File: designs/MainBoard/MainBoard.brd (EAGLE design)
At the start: 86 x 37 mm, 6 parts

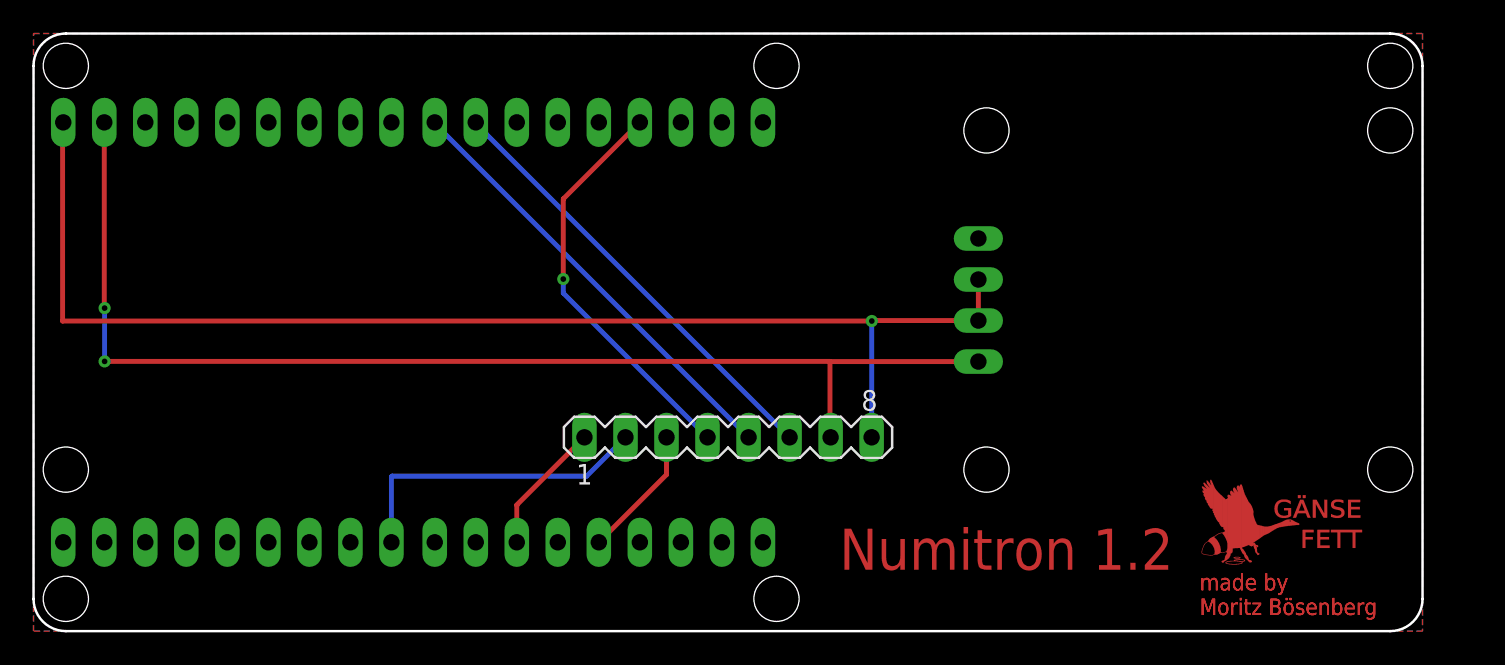
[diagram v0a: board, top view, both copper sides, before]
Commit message: added correct measurements
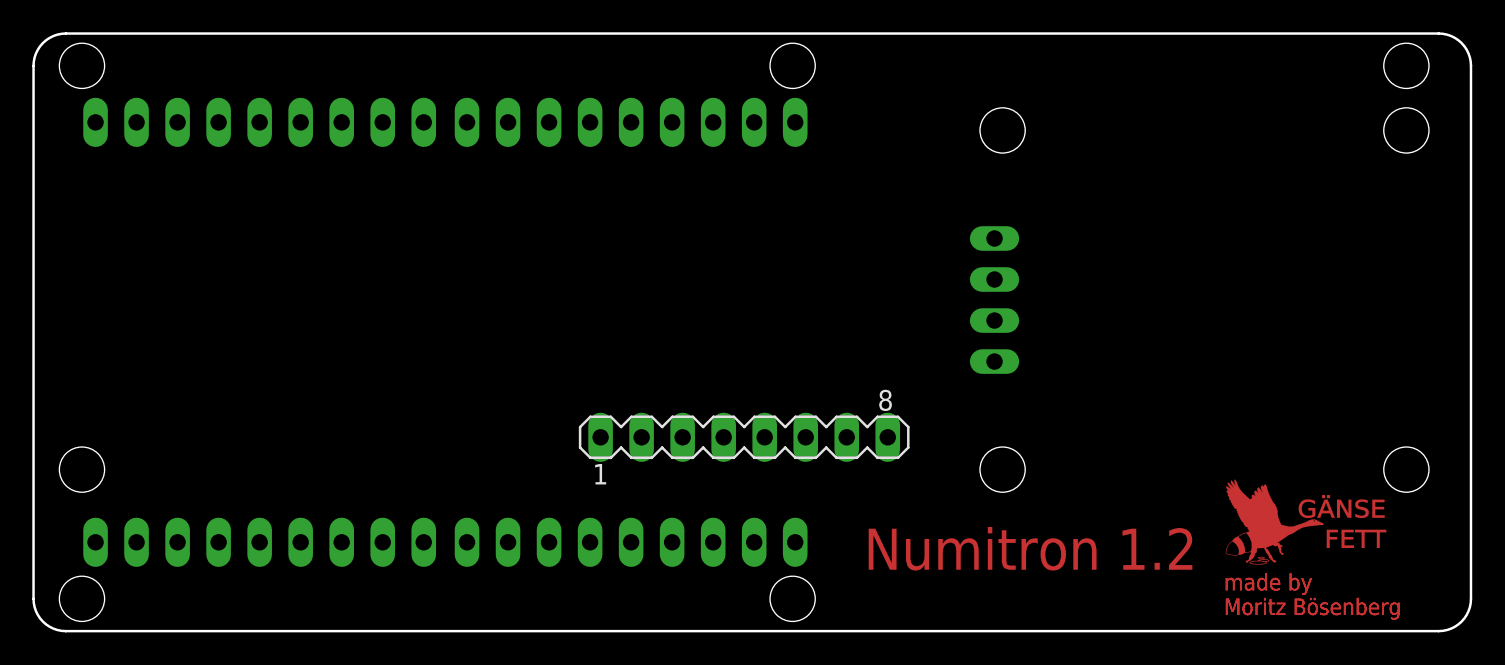
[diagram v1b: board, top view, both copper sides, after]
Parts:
- moved SV2 2.00 mm to (37.0, 5.50)
- moved SV3 2.00 mm to (14.0, 5.50)
- moved SV5 2.00 mm to (14.0, 31.5)
- moved SV6 2.00 mm to (37.0, 31.5)
- moved JP1 1.00 mm to (59.5, 20.5)
- moved SV1 1.00 mm to (44.0, 12.0)
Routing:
- net GND: track 78.8 -> 0.00 mm, vias 1 -> 0
- net 3.3V: track 73.6 -> 0.00 mm, vias 2 -> 0
- net IO26: track 27.5 -> 0.00 mm
- net IO25: track 27.5 -> 0.00 mm
- net GPIO13: track 25.2 -> 0.00 mm, vias 1 -> 0
- net IO5: track 19.6 -> 0.00 mm
- net IO4: track 8.24 -> 0.00 mm
- net IO2: track 8.24 -> 0.00 mm
- removed copper zone on layer 1, net GND
- removed copper zone on layer 16, net GND
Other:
- board size 86 x 37 mm -> 89 x 37 mm

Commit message: finished mainboard
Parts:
- removed SV1: (no value), con-lstb:MA08-1
- added J1, J2, J3, J4, J5, J6, J7, J8: S2B-PH-SM4, CommonParts:JST_S2B-PH-SM4-TB(LF)(SN)
- added R1, R2, R3, R4: (no value), CommonParts:R1206
- added SV4: (no value), CommonParts:MA08-1
- moved JP1 1.00 mm to (58.5, 20.5)
- moved SV2 1.00 mm to (36.0, 5.50)
- moved SV3 1.00 mm to (13.0, 5.50)
- moved SV5 1.00 mm to (13.0, 31.5)
- moved SV6 1.00 mm to (36.0, 31.5)
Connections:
- net 3.3V: now also J2.1, J4.1, J6.1, J8.1, R1.1, R2.1, R3.1, R4.1, SV4.7; no longer SV1.7
- net GND: now also J1.2, J2.2, J3.2, J4.2, J5.2, J6.2, J7.2, J8.2, SV4.8; no longer SV1.8
- net GPIO13: now also SV4.4; no longer SV1.4
- net IO15: now also J1.1, R1.2
- net IO2: now also SV4.3; no longer SV1.3
- net IO22: now also J7.1, R4.2
- net IO25: now also SV4.5; no longer SV1.5
- net IO26: now also SV4.6; no longer SV1.6
- net IO4: now also SV4.1; no longer SV1.1
- net IO5: now also SV4.2; no longer SV1.2
- net RXD0: now also J3.1, R2.2
- net TXD0: now also J5.1, R3.2
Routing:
- net GND: track 0.00 -> 173.4 mm, vias 0 -> 3
- net 3.3V: track 0.00 -> 119.9 mm, vias 0 -> 3
- net TXD0: track 0.00 -> 100.5 mm, vias 0 -> 4
- net IO22: track 0.00 -> 89.8 mm
- net RXD0: track 0.00 -> 87.3 mm, vias 0 -> 3
- net IO15: track 0.00 -> 52.1 mm, vias 0 -> 1
- net GPIO13: track 0.00 -> 49.7 mm, vias 0 -> 1
- net IO25: track 0.00 -> 35.6 mm, vias 0 -> 1
- net IO26: track 0.00 -> 34.7 mm, vias 0 -> 1
- net IO4: track 0.00 -> 18.6 mm
- net IO5: track 0.00 -> 17.9 mm
- net IO2: track 0.00 -> 8.36 mm
- added copper zone on layer 1, net GND
- added copper zone on layer 16, net GND
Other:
- board size 89 x 37 mm -> 86 x 37 mm
- board text added: "3.3V"
- board text added: "CLK"
- board text added: "CMD"
- board text added: "GND"
- board text added: "GPIO12"
- board text added: "GPIO13"
- board text added: "GPIO14"
- board text added: "IO0"
- board text added: "IO15"
- board text added: "IO18"
- board text added: "IO19"
- board text added: "IO2"
- board text added: "IO21"
- board text added: "IO22"
- board text added: "IO23"
- board text added: "IO25"
- board text added: "IO26"
- board text added: "IO27"
- board text added: "IO32"
- board text added: "IO33"
- board text added: "IO34"
- board text added: "IO35"
- board text added: "IO4"
- board text added: "IO5"
- board text added: "NC"
- board text added: "NC_1"
- board text added: "NC_2"
- board text added: "NC_3"
- board text added: "RXD0"
- board text added: "SD0"
- board text added: "SD1"
- board text added: "SD2"
- board text added: "SD3"
- board text added: "SEN_VN"
- board text added: "SEN_VP"
- board text added: "TXD0"

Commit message: added last design tunes
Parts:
- R1, R2, R3, R4: value (none) -> 10K
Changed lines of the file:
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@@
 <setting verticaltext="up"/>
 </settings>
-<grid distance="0.5" unitdist="mm" unit="mm" style="lines" multiple="1" display="no" altdistance="5" altunitdist="mil" altunit="mil"/>
+<grid distance="0.1" unitdist="mm" unit="mm" style="lines" multiple="1" display="no" altdistance="5" altunitdist="mil" altunit="mil"/>
 <layers>
 <layer number="1" name="Top" color="4" fill="1" visible="yes" active="yes"/>
@@
 </class>
 </classes>
-<designrules name="default *">
+<designrules name="Main_1">
 <description language="de">&lt;b&gt;EAGLE Design Rules&lt;/b&gt;
 &lt;p&gt;
@@
 <param name="mdViaViaSameLayer" value="6mil"/>
 <param name="mnLayersViaInSmd" value="2"/>
-<param name="mdCopperDimension" value="20mil"/>
+<param name="mdCopperDimension" value="10mil"/>
 <param name="mdDrill" value="6mil"/>
 <param name="mdSmdStop" value="0mil"/>
@@
 <attribute name="PACKAGE" value="None" x="68.5" y="29" size="1.778" layer="28" rot="MR180" display="off"/>
 </element>
-<element name="R1" library="CommonParts" package="R1206" package3d_urn="urn:adsk.eagle:package:23540/2" value="" x="73" y="14.5" smashed="yes">
+<element name="R1" library="CommonParts" package="R1206" package3d_urn="urn:adsk.eagle:package:23540/2" value="10K" x="73" y="14.5" smashed="yes">
 <attribute name="NAME" x="71.73" y="15.77" size="0.8128" layer="25"/>
-<attribute name="VALUE" x="71.73" y="11.96" size="1.27" layer="27"/>
+<attribute name="VALUE" x="71.73" y="12.46" size="0.8128" layer="27"/>
 </element>
-<element name="R2" library="CommonParts" package="R1206" package3d_urn="urn:adsk.eagle:package:23540/2" value="" x="73" y="14.5" smashed="yes" rot="MR0">
+<element name="R2" library="CommonParts" package="R1206" package3d_urn="urn:adsk.eagle:package:23540/2" value="10K" x="73" y="14.5" smashed="yes" rot="MR0">
 <attribute name="NAME" x="74.27" y="15.77" size="0.8128" layer="26" rot="MR0"/>
-<attribute name="VALUE" x="74.27" y="11.96" size="1.27" layer="28" rot="MR0"/>
+<attribute name="VALUE" x="74.27" y="12.46" size="0.8128" layer="28" rot="MR0"/>
 </element>
-<element name="R3" library="CommonParts" package="R1206" package3d_urn="urn:adsk.eagle:package:23540/2" value="" x="73" y="22.5" smashed="yes">
+<element name="R3" library="CommonParts" package="R1206" package3d_urn="urn:adsk.eagle:package:23540/2" value="10K" x="73" y="22.5" smashed="yes">
 <attribute name="NAME" x="71.73" y="23.77" size="0.8128" layer="25"/>
-<attribute name="VALUE" x="71.73" y="19.96" size="1.27" layer="27"/>
+<attribute name="VALUE" x="71.73" y="20.46" size="0.8128" layer="27"/>
 </element>
-<element name="R4" library="CommonParts" package="R1206" package3d_urn="urn:adsk.eagle:package:23540/2" value="" x="73" y="22.5" smashed="yes" rot="MR0">
+<element name="R4" library="CommonParts" package="R1206" package3d_urn="urn:adsk.eagle:package:23540/2" value="10K" x="73" y="22.5" smashed="yes" rot="MR0">
 <attribute name="NAME" x="74.27" y="23.77" size="0.8128" layer="26" rot="MR0"/>
-<attribute name="VALUE" x="74.27" y="19.96" size="1.27" layer="28" rot="MR0"/>
+<attribute name="VALUE" x="73.77" y="20.46" size="0.8128" layer="28" rot="MR0"/>
 </element>
 <element name="SV4" library="CommonParts" package="MA08-1" package3d_urn="urn:adsk.eagle:package:8343/1" value="" x="43" y="12" smashed="yes">
